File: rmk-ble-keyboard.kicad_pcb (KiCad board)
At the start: 2 copper layers, 57.8 x 48.1 mm, 1 part

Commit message: add matrix
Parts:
- added D1: 1N4148W, Diode_SMD:D_SOD-123, B.Cu at (41.2, 38.1)
- added D10: 1N4148W, Diode_SMD:D_SOD-123, B.Cu at (212.7, 38.1)
- added D11: 1N4148W, Diode_SMD:D_SOD-123, B.Cu at (231.7, 38.1)
- added D12: 1N4148W, Diode_SMD:D_SOD-123, B.Cu at (250.8, 38.1)
- added D13: 1N4148W, Diode_SMD:D_SOD-123, B.Cu at (269.8, 38.1)
- added D14: 1N4148W, Diode_SMD:D_SOD-123, B.Cu at (298.4, 38.1)
- added D15: 1N4148W, Diode_SMD:D_SOD-123, B.Cu at (46.0, 57.1)
- added D16: 1N4148W, Diode_SMD:D_SOD-123, B.Cu at (69.8, 57.1)
- added D17: 1N4148W, Diode_SMD:D_SOD-123, B.Cu at (88.8, 57.1)
- added D18: 1N4148W, Diode_SMD:D_SOD-123, B.Cu at (107.9, 57.1)
- added D19: 1N4148W, Diode_SMD:D_SOD-123, B.Cu at (126.9, 57.1)
- added D2: 1N4148W, Diode_SMD:D_SOD-123, B.Cu at (60.2, 38.1)
- added D20: 1N4148W, Diode_SMD:D_SOD-123, B.Cu at (146.0, 57.1)
- added D21: 1N4148W, Diode_SMD:D_SOD-123, B.Cu at (165.0, 57.1)
- added D22: 1N4148W, Diode_SMD:D_SOD-123, B.Cu at (184.1, 57.1)
- added D23: 1N4148W, Diode_SMD:D_SOD-123, B.Cu at (203.1, 57.1)
- added D24: 1N4148W, Diode_SMD:D_SOD-123, B.Cu at (222.2, 57.1)
- added D25: 1N4148W, Diode_SMD:D_SOD-123, B.Cu at (241.2, 57.1)
- added D26: 1N4148W, Diode_SMD:D_SOD-123, B.Cu at (260.3, 57.1)
- added D27: 1N4148W, Diode_SMD:D_SOD-123, B.Cu at (279.3, 57.1)
- added D28: 1N4148W, Diode_SMD:D_SOD-123, B.Cu at (303.1, 57.1)
- added D29: 1N4148W, Diode_SMD:D_SOD-123, B.Cu at (48.3, 76.2)
- added D3: 1N4148W, Diode_SMD:D_SOD-123, B.Cu at (79.3, 38.1)
- added D30: 1N4148W, Diode_SMD:D_SOD-123, B.Cu at (74.5, 76.2)
- added D31: 1N4148W, Diode_SMD:D_SOD-123, B.Cu at (93.6, 76.2)
- added D32: 1N4148W, Diode_SMD:D_SOD-123, B.Cu at (112.6, 76.2)
- added D33: 1N4148W, Diode_SMD:D_SOD-123, B.Cu at (131.7, 76.2)
- added D34: 1N4148W, Diode_SMD:D_SOD-123, B.Cu at (150.7, 76.2)
- added D35: 1N4148W, Diode_SMD:D_SOD-123, B.Cu at (169.8, 76.2)
- added D36: 1N4148W, Diode_SMD:D_SOD-123, B.Cu at (188.8, 76.2)
- added D37: 1N4148W, Diode_SMD:D_SOD-123, B.Cu at (207.9, 76.2)
- added D38: 1N4148W, Diode_SMD:D_SOD-123, B.Cu at (226.9, 76.2)
- added D39: 1N4148W, Diode_SMD:D_SOD-123, B.Cu at (246.0, 76.2)
- added D4: 1N4148W, Diode_SMD:D_SOD-123, B.Cu at (98.3, 38.1)
- added D40: 1N4148W, Diode_SMD:D_SOD-123, B.Cu at (265.0, 76.2)
- added D41: 1N4148W, Diode_SMD:D_SOD-123, B.Cu at (53.1, 95.2)
- added D42: 1N4148W, Diode_SMD:D_SOD-123, B.Cu at (296.0, 76.2)
- added D43: 1N4148W, Diode_SMD:D_SOD-123, B.Cu at (84.1, 95.2)
- added D44: 1N4148W, Diode_SMD:D_SOD-123, B.Cu at (103.1, 95.2)
- added D45: 1N4148W, Diode_SMD:D_SOD-123, B.Cu at (122.2, 95.2)
- added D46: 1N4148W, Diode_SMD:D_SOD-123, B.Cu at (141.2, 95.2)
- added D47: 1N4148W, Diode_SMD:D_SOD-123, B.Cu at (160.3, 95.2)
- added D48: 1N4148W, Diode_SMD:D_SOD-123, B.Cu at (179.3, 95.2)
- added D49: 1N4148W, Diode_SMD:D_SOD-123, B.Cu at (198.4, 95.2)
- added D5: 1N4148W, Diode_SMD:D_SOD-123, B.Cu at (117.4, 38.1)
- added D50: 1N4148W, Diode_SMD:D_SOD-123, B.Cu at (217.4, 95.2)
- added D51: 1N4148W, Diode_SMD:D_SOD-123, B.Cu at (236.5, 95.2)
- added D52: 1N4148W, Diode_SMD:D_SOD-123, B.Cu at (255.5, 95.2)
- added D53: 1N4148W, Diode_SMD:D_SOD-123, B.Cu at (291.2, 95.2)
- added D54: 1N4148W, Diode_SMD:D_SOD-123, B.Cu at (43.6, 114.3)
- added D55: 1N4148W, Diode_SMD:D_SOD-123, B.Cu at (67.4, 114.3)
- added D56: 1N4148W, Diode_SMD:D_SOD-123, B.Cu at (91.2, 114.3)
- added D57: 1N4148W, Diode_SMD:D_SOD-123, B.Cu at (162.6, 114.3)
- added D58: 1N4148W, Diode_SMD:D_SOD-123, B.Cu at (234.1, 114.3)
- added D59: 1N4148W, Diode_SMD:D_SOD-123, B.Cu at (257.9, 114.3)
- added D6: 1N4148W, Diode_SMD:D_SOD-123, B.Cu at (136.4, 38.1)
- added D60: 1N4148W, Diode_SMD:D_SOD-123, B.Cu at (281.7, 114.3)
- added D61: 1N4148W, Diode_SMD:D_SOD-123, B.Cu at (305.5, 114.3)
- added D7: 1N4148W, Diode_SMD:D_SOD-123, B.Cu at (155.5, 38.1)
- added D8: 1N4148W, Diode_SMD:D_SOD-123, B.Cu at (174.6, 38.1)
- added D9: 1N4148W, Diode_SMD:D_SOD-123, B.Cu at (193.6, 38.1)
- added SW1: esc, PCM_Switch_Keyboard_Hotswap_Kailh:SW_Hotswap_Kailh_MX_Plated_1.00u, F.Cu at (38.1, 38.1)
- added SW10: 9, PCM_Switch_Keyboard_Hotswap_Kailh:SW_Hotswap_Kailh_MX_Plated_1.00u, F.Cu at (209.6, 38.1)
- added SW11: 0, PCM_Switch_Keyboard_Hotswap_Kailh:SW_Hotswap_Kailh_MX_Plated_1.00u, F.Cu at (228.6, 38.1)
- added SW12: -, PCM_Switch_Keyboard_Hotswap_Kailh:SW_Hotswap_Kailh_MX_Plated_1.00u, F.Cu at (247.7, 38.1)
- added SW13: =, PCM_Switch_Keyboard_Hotswap_Kailh:SW_Hotswap_Kailh_MX_Plated_1.00u, F.Cu at (266.7, 38.1)
- added SW14: backspace, PCM_Switch_Keyboard_Hotswap_Kailh:SW_Hotswap_Kailh_MX_Plated_2.00u, F.Cu at (295.3, 38.1)
- added SW15: tab, PCM_Switch_Keyboard_Hotswap_Kailh:SW_Hotswap_Kailh_MX_Plated_1.50u, F.Cu at (42.9, 57.1)
- added SW16: q, PCM_Switch_Keyboard_Hotswap_Kailh:SW_Hotswap_Kailh_MX_Plated_1.00u, F.Cu at (66.7, 57.1)
- added SW17: w, PCM_Switch_Keyboard_Hotswap_Kailh:SW_Hotswap_Kailh_MX_Plated_1.00u, F.Cu at (85.7, 57.1)
- added SW18: e, PCM_Switch_Keyboard_Hotswap_Kailh:SW_Hotswap_Kailh_MX_Plated_1.00u, F.Cu at (104.8, 57.1)
- added SW19: r, PCM_Switch_Keyboard_Hotswap_Kailh:SW_Hotswap_Kailh_MX_Plated_1.00u, F.Cu at (123.8, 57.1)
- added SW2: 1, PCM_Switch_Keyboard_Hotswap_Kailh:SW_Hotswap_Kailh_MX_Plated_1.00u, F.Cu at (57.1, 38.1)
- added SW20: t, PCM_Switch_Keyboard_Hotswap_Kailh:SW_Hotswap_Kailh_MX_Plated_1.00u, F.Cu at (142.9, 57.1)
- added SW21: y, PCM_Switch_Keyboard_Hotswap_Kailh:SW_Hotswap_Kailh_MX_Plated_1.00u, F.Cu at (161.9, 57.1)
- added SW22: u, PCM_Switch_Keyboard_Hotswap_Kailh:SW_Hotswap_Kailh_MX_Plated_1.00u, F.Cu at (181.0, 57.1)
- added SW23: i, PCM_Switch_Keyboard_Hotswap_Kailh:SW_Hotswap_Kailh_MX_Plated_1.00u, F.Cu at (200.0, 57.1)
- added SW24: o, PCM_Switch_Keyboard_Hotswap_Kailh:SW_Hotswap_Kailh_MX_Plated_1.00u, F.Cu at (219.1, 57.1)
- added SW25: p, PCM_Switch_Keyboard_Hotswap_Kailh:SW_Hotswap_Kailh_MX_Plated_1.00u, F.Cu at (238.1, 57.1)
- added SW26: [, PCM_Switch_Keyboard_Hotswap_Kailh:SW_Hotswap_Kailh_MX_Plated_1.00u, F.Cu at (257.2, 57.1)
- added SW27: ], PCM_Switch_Keyboard_Hotswap_Kailh:SW_Hotswap_Kailh_MX_Plated_1.00u, F.Cu at (276.2, 57.1)
- added SW28: \, PCM_Switch_Keyboard_Hotswap_Kailh:SW_Hotswap_Kailh_MX_Plated_1.50u, F.Cu at (300.0, 57.1)
- added SW29: capslock, PCM_Switch_Keyboard_Hotswap_Kailh:SW_Hotswap_Kailh_MX_Plated_1.75u, F.Cu at (45.2, 76.2)
- added SW3: 2, PCM_Switch_Keyboard_Hotswap_Kailh:SW_Hotswap_Kailh_MX_Plated_1.00u, F.Cu at (76.2, 38.1)
- added SW30: a, PCM_Switch_Keyboard_Hotswap_Kailh:SW_Hotswap_Kailh_MX_Plated_1.00u, F.Cu at (71.4, 76.2)
- added SW31: s, PCM_Switch_Keyboard_Hotswap_Kailh:SW_Hotswap_Kailh_MX_Plated_1.00u, F.Cu at (90.5, 76.2)
- added SW32: d, PCM_Switch_Keyboard_Hotswap_Kailh:SW_Hotswap_Kailh_MX_Plated_1.00u, F.Cu at (109.5, 76.2)
- added SW33: f, PCM_Switch_Keyboard_Hotswap_Kailh:SW_Hotswap_Kailh_MX_Plated_1.00u, F.Cu at (128.6, 76.2)
- added SW34: g, PCM_Switch_Keyboard_Hotswap_Kailh:SW_Hotswap_Kailh_MX_Plated_1.00u, F.Cu at (147.6, 76.2)
- added SW35: h, PCM_Switch_Keyboard_Hotswap_Kailh:SW_Hotswap_Kailh_MX_Plated_1.00u, F.Cu at (166.7, 76.2)
- added SW36: j, PCM_Switch_Keyboard_Hotswap_Kailh:SW_Hotswap_Kailh_MX_Plated_1.00u, F.Cu at (185.7, 76.2)
- added SW37: k, PCM_Switch_Keyboard_Hotswap_Kailh:SW_Hotswap_Kailh_MX_Plated_1.00u, F.Cu at (204.8, 76.2)
- added SW38: l, PCM_Switch_Keyboard_Hotswap_Kailh:SW_Hotswap_Kailh_MX_Plated_1.00u, F.Cu at (223.8, 76.2)
- added SW39: ;, PCM_Switch_Keyboard_Hotswap_Kailh:SW_Hotswap_Kailh_MX_Plated_1.00u, F.Cu at (242.9, 76.2)
- added SW4: 3, PCM_Switch_Keyboard_Hotswap_Kailh:SW_Hotswap_Kailh_MX_Plated_1.00u, F.Cu at (95.2, 38.1)
- added SW40: ', PCM_Switch_Keyboard_Hotswap_Kailh:SW_Hotswap_Kailh_MX_Plated_1.00u, F.Cu at (261.9, 76.2)
- added SW41: enter, PCM_Switch_Keyboard_Hotswap_Kailh:SW_Hotswap_Kailh_MX_Plated_2.25u, F.Cu at (292.9, 76.2)
- added SW42: lshift, PCM_Switch_Keyboard_Hotswap_Kailh:SW_Hotswap_Kailh_MX_Plated_2.25u, F.Cu at (50.0, 95.2)
- added SW43: z, PCM_Switch_Keyboard_Hotswap_Kailh:SW_Hotswap_Kailh_MX_Plated_1.00u, F.Cu at (81.0, 95.2)
- added SW44: x, PCM_Switch_Keyboard_Hotswap_Kailh:SW_Hotswap_Kailh_MX_Plated_1.00u, F.Cu at (100.0, 95.2)
- added SW45: c, PCM_Switch_Keyboard_Hotswap_Kailh:SW_Hotswap_Kailh_MX_Plated_1.00u, F.Cu at (119.1, 95.2)
- added SW46: v, PCM_Switch_Keyboard_Hotswap_Kailh:SW_Hotswap_Kailh_MX_Plated_1.00u, F.Cu at (138.1, 95.2)
- added SW47: b, PCM_Switch_Keyboard_Hotswap_Kailh:SW_Hotswap_Kailh_MX_Plated_1.00u, F.Cu at (157.2, 95.2)
- added SW48: n, PCM_Switch_Keyboard_Hotswap_Kailh:SW_Hotswap_Kailh_MX_Plated_1.00u, F.Cu at (176.2, 95.2)
- added SW49: m, PCM_Switch_Keyboard_Hotswap_Kailh:SW_Hotswap_Kailh_MX_Plated_1.00u, F.Cu at (195.3, 95.2)
- added SW5: 4, PCM_Switch_Keyboard_Hotswap_Kailh:SW_Hotswap_Kailh_MX_Plated_1.00u, F.Cu at (114.3, 38.1)
- added SW50: ,, PCM_Switch_Keyboard_Hotswap_Kailh:SW_Hotswap_Kailh_MX_Plated_1.00u, F.Cu at (214.3, 95.2)
- added SW51: ., PCM_Switch_Keyboard_Hotswap_Kailh:SW_Hotswap_Kailh_MX_Plated_1.00u, F.Cu at (233.4, 95.2)
- added SW52: /, PCM_Switch_Keyboard_Hotswap_Kailh:SW_Hotswap_Kailh_MX_Plated_1.00u, F.Cu at (252.4, 95.2)
- added SW53: rshift, PCM_Switch_Keyboard_Hotswap_Kailh:SW_Hotswap_Kailh_MX_Plated_2.75u, F.Cu at (288.1, 95.2)
- added SW54: lctrl, PCM_Switch_Keyboard_Hotswap_Kailh:SW_Hotswap_Kailh_MX_Plated_1.25u, F.Cu at (40.5, 114.3)
- added SW55: lgui, PCM_Switch_Keyboard_Hotswap_Kailh:SW_Hotswap_Kailh_MX_Plated_1.25u, F.Cu at (64.3, 114.3)
- added SW56: lalt, PCM_Switch_Keyboard_Hotswap_Kailh:SW_Hotswap_Kailh_MX_Plated_1.25u, F.Cu at (88.1, 114.3)
- added SW57: space, PCM_Switch_Keyboard_Hotswap_Kailh:SW_Hotswap_Kailh_MX_Plated_6.25u, F.Cu at (159.5, 114.3)
- added SW58: ralt, PCM_Switch_Keyboard_Hotswap_Kailh:SW_Hotswap_Kailh_MX_Plated_1.25u, F.Cu at (231.0, 114.3)
- added SW59: rgui, PCM_Switch_Keyboard_Hotswap_Kailh:SW_Hotswap_Kailh_MX_Plated_1.25u, F.Cu at (254.8, 114.3)
- added SW6: 5, PCM_Switch_Keyboard_Hotswap_Kailh:SW_Hotswap_Kailh_MX_Plated_1.00u, F.Cu at (133.3, 38.1)
- added SW60: fn, PCM_Switch_Keyboard_Hotswap_Kailh:SW_Hotswap_Kailh_MX_Plated_1.25u, F.Cu at (278.6, 114.3)
- added SW61: rctrl, PCM_Switch_Keyboard_Hotswap_Kailh:SW_Hotswap_Kailh_MX_Plated_1.25u, F.Cu at (302.4, 114.3)
- added SW7: 6, PCM_Switch_Keyboard_Hotswap_Kailh:SW_Hotswap_Kailh_MX_Plated_1.00u, F.Cu at (152.4, 38.1)
- added SW8: 7, PCM_Switch_Keyboard_Hotswap_Kailh:SW_Hotswap_Kailh_MX_Plated_1.00u, F.Cu at (171.4, 38.1)
- added SW9: 8, PCM_Switch_Keyboard_Hotswap_Kailh:SW_Hotswap_Kailh_MX_Plated_1.00u, F.Cu at (190.5, 38.1)
- moved U1 92.4 mm to (153.1, 176.4)
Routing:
- net col2: track 0.00 -> 88.4 mm
- net col3: track 0.00 -> 86.4 mm
- net col10: track 0.00 -> 83.6 mm
- net col6: track 0.00 -> 83.6 mm
- net col11: track 0.00 -> 83.6 mm
- net col1: track 0.00 -> 81.6 mm
- net col13: track 0.00 -> 80.0 mm
- net col8: track 0.00 -> 63.6 mm
- net col5: track 0.00 -> 63.6 mm
- net col4: track 0.00 -> 63.6 mm
- net col9: track 0.00 -> 63.6 mm
- net col7: track 0.00 -> 63.6 mm
- net col14: track 0.00 -> 60.6 mm
- net col12: track 0.00 -> 41.7 mm
- net Net-(D61-A): track 0.00 -> 3.66 mm
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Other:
- board outline removed

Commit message: add usb & esd
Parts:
- added U2: USBLC6-2SC6, Package_TO_SOT_SMD:SOT-23-6, F.Cu at (203.6, 112.2)
- U1: moved to B.Cu
- moved U1 59.1 mm to (132.6, 120.9), turned to 180 degrees
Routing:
- net row4: track 0.00 -> 242.2 mm
- net row5: track 0.00 -> 48.4 mm
- net col14: track 60.6 -> 85.9 mm
- net col2: track 88.4 -> 89.9 mm
- net col3: track 86.4 -> 87.4 mm
- net col1: track 81.6 -> 82.4 mm
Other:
- board outline added: 285 x 94.5 mm

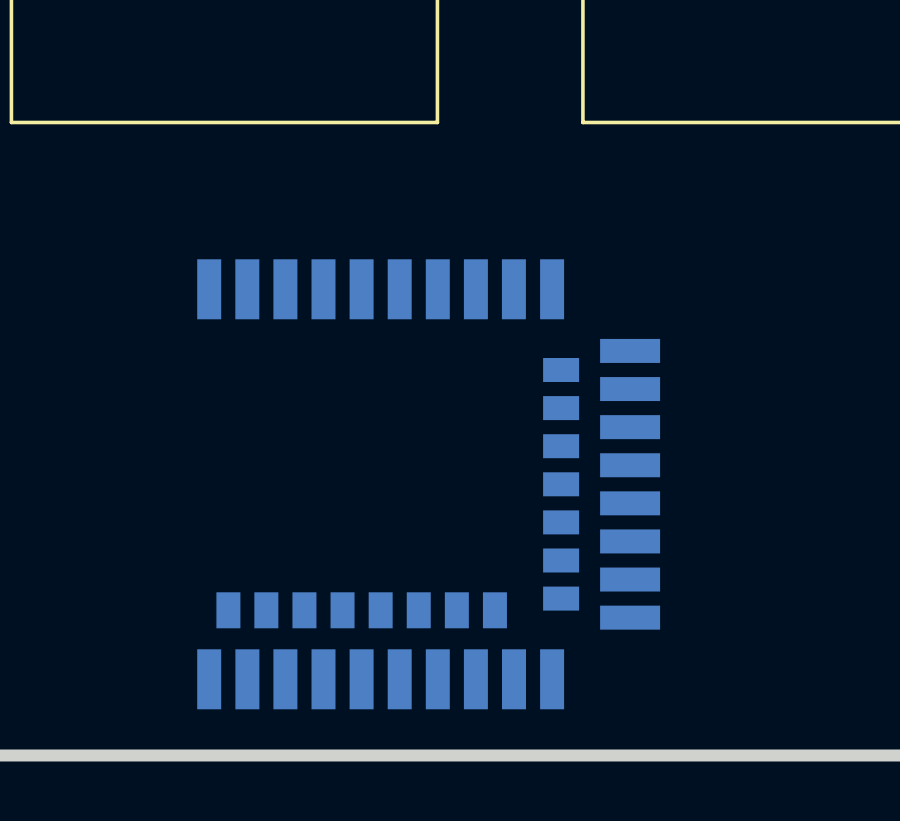
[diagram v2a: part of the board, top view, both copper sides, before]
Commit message: add e73 pin out in schema
Signed-off-by: HaoboGu <haobogu@outlook.com>
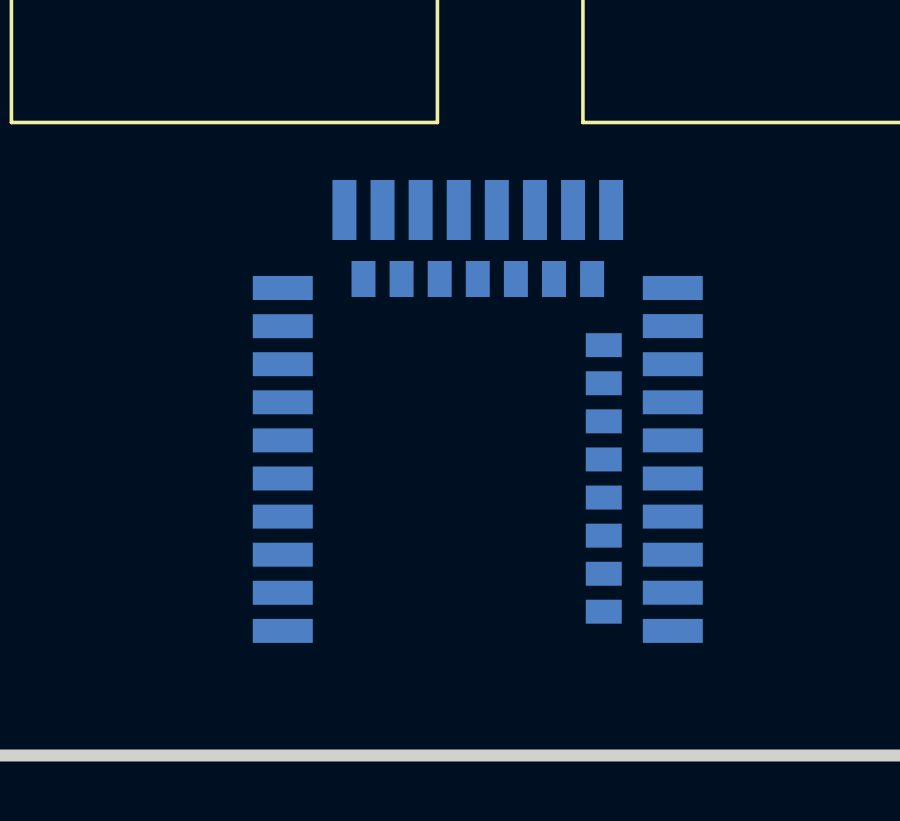
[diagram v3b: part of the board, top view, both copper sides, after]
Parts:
- moved U1 15.7 mm to (134.0, 105.3), turned to -90 degrees
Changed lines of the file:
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@@
 	(footprint "E73_2G4M08S1C:E73(2G4M08S1C)"
 		(layer "B.Cu")
-		(at 132.585 120.91 180)
+		(at 134.008 105.267 -90)
 		(property "Reference" "U1"
-			(at 8.525 14.7003 0)
+			(at 8.525 14.7003 90)
 			(unlocked yes)
 			(layer "B.SilkS")
@@
 		)
 		(property "Value" "~"
-			(at 8.525 -1.7003 0)
+			(at 8.525 -1.7003 90)
 			(unlocked yes)
 			(layer "B.Fab")
@@
 		)
 		(property "Footprint" "E73_2G4M08S1C:E73(2G4M08S1C)"
-			(at 0 0 0)
+			(at 0 0 90)
 			(unlocked yes)
 			(layer "B.Fab")
@@
 		)
 		(property "Datasheet" ""
-			(at 0 0 0)
+			(at 0 0 90)
 			(unlocked yes)
 			(layer "B.Fab")
@@
 		)
 		(property "Description" ""
-			(at 0 0 0)
+			(at 0 0 90)
 			(unlocked yes)
 			(layer "B.Fab")
@@
 		(sheetfile "rmk-ble-keyboard.kicad_sch")
 		(fp_line
-			(start 18 13)
-			(end 18 0)
+			(start 0 13)
+			(end 0 0)
 			(stroke
 				(width 0.1)
@@
 		)
 		(fp_line
+			(start 18 13)
+			(end 18 0)
+			(stroke
+				(width 0.1)
+				(type solid)
+			)
+			(layer "B.SilkS")
+		)
+		(fp_line
 			(start 18 0)
 			(end 0 0)
@@
 			(layer "B.SilkS")
 		)
-		(fp_line
-			(start 0 13)
-			(end 0 0)
-			(stroke
-				(width 0.1)
-				(type solid)
-			)
-			(layer "B.SilkS")
-		)
 		(pad "1" smd rect
-			(at 14.03 13 270)
+			(at 14.03 13)
 			(size 2 0.8)
 			(layers "B.Cu" "B.Paste" "B.Mask")
@@
 		)
 		(pad "2" smd rect
-			(at 12.76 13 270)
+			(at 12.76 13)
 			(size 2 0.8)
 			(layers "B.Cu" "B.Paste" "B.Mask")
@@
 		)
 		(pad "3" smd rect
-			(at 11.49 13 270)
+			(at 11.49 13)
 			(size 2 0.8)
 			(layers "B.Cu" "B.Paste" "B.Mask")
@@
 		)
 		(pad "4" smd rect
-			(at 10.22 13 270)
+			(at 10.22 13)
 			(size 2 0.8)
 			(layers "B.Cu" "B.Paste" "B.Mask")
@@
 		)
 		(pad "5" smd rect
-			(at 8.95 13 270)
+			(at 8.95 13)
 			(size 2 0.8)
 			(layers "B.Cu" "B.Paste" "B.Mask")
@@
 		)
 		(pad "6" smd rect
-			(at 7.68 13 270)
+			(at 7.68 13)
 			(size 2 0.8)
 			(layers "B.Cu" "B.Paste" "B.Mask")
@@
 		)
 		(pad "7" smd rect
-			(at 6.41 13 270)
+			(at 6.41 13)
 			(size 2 0.8)
 			(layers "B.Cu" "B.Paste" "B.Mask")
@@
 		)
 		(pad "8" smd rect
-			(at 5.14 13 270)
+			(at 5.14 13)
 			(size 2 0.8)
 			(layers "B.Cu" "B.Paste" "B.Mask")
@@
 		)
 		(pad "9" smd rect
-			(at 3.8728 13.0003 270)
+			(at 3.8728 13.0003)
 			(size 2 0.8)
 			(layers "B.Cu" "B.Paste" "B.Mask")
@@
 		)
 		(pad "10" smd rect
-			(at 2.6 13 270)
+			(at 2.6 13)
 			(size 2 0.8)
 			(layers "B.Cu" "B.Paste" "B.Mask")
@@
 		)
 		(pad "11" smd rect
-			(at 0 10.945 180)
+			(at 0 10.945 270)
 			(size 2 0.8)
 			(layers "B.Cu" "B.Paste" "B.Mask")
@@
 		)
 		(pad "12" smd rect
-			(at 2.3 10.30975 180)
+			(at 2.3 10.30975 270)
 			(size 1.2 0.8)
 			(layers "B.Cu" "B.Paste" "B.Mask")
@@
 		)
 		(pad "13" smd rect
-			(at 0 9.675 180)
+			(at 0 9.675 270)
 			(size 2 0.8)
 			(layers "B.Cu" "B.Paste" "B.Mask")
@@
 		)
 		(pad "14" smd rect
-			(at 2.3 9.03975 180)
+			(at 2.3 9.03975 270)
 			(size 1.2 0.8)
 			(layers "B.Cu" "B.Paste" "B.Mask")
@@
 		)
 		(pad "15" smd rect
-			(at 0 8.405 180)
+			(at 0 8.405 270)
 			(size 2 0.8)
 			(layers "B.Cu" "B.Paste" "B.Mask")
@@
 		)
 		(pad "16" smd rect
-			(at 2.3 7.76975 180)
+			(at 2.3 7.76975 270)
 			(size 1.2 0.8)
 			(layers "B.Cu" "B.Paste" "B.Mask")
@@
 		)
 		(pad "17" smd rect
-			(at 0 7.135 180)
+			(at 0 7.135 270)
 			(size 2 0.8)
 			(layers "B.Cu" "B.Paste" "B.Mask")
@@
 		)
 		(pad "18" smd rect
-			(at 2.3 6.49975 180)
+			(at 2.3 6.49975 270)
 			(size 1.2 0.8)
 			(layers "B.Cu" "B.Paste" "B.Mask")
@@
 		)
 		(pad "19" smd rect
-			(at 0 5.865 180)
+			(at 0 5.865 270)
 			(size 2 0.8)
 			(layers "B.Cu" "B.Paste" "B.Mask")
@@
 		)
 		(pad "20" smd rect
-			(at 2.3 5.22975 180)
+			(at 2.3 5.22975 270)
 			(size 1.2 0.8)
 			(layers "B.Cu" "B.Paste" "B.Mask")
@@
 		)
 		(pad "21" smd rect
-			(at 0 4.595 180)
+			(at 0 4.595 270)
 			(size 2 0.8)
 			(layers "B.Cu" "B.Paste" "B.Mask")
@@
 		)
 		(pad "22" smd rect
-			(at 2.3 3.95975 180)
+			(at 2.3 3.95975 270)
 			(size 1.2 0.8)
 			(layers "B.Cu" "B.Paste" "B.Mask")
@@
 		)
 		(pad "23" smd rect
-			(at 0 3.325 180)
+			(at 0 3.325 270)
 			(size 2 0.8)
 			(layers "B.Cu" "B.Paste" "B.Mask")
@@
 		)
 		(pad "24" smd rect
-			(at 2.3 2.69 180)
+			(at 2.3 2.69 270)
 			(size 1.2 0.8)
 			(layers "B.Cu" "B.Paste" "B.Mask")
@@
 		)
 		(pad "25" smd rect
-			(at 0 2.055 180)
+			(at 0 2.055 270)
 			(size 2 0.8)
 			(layers "B.Cu" "B.Paste" "B.Mask")
@@
 		)
 		(pad "26" smd rect
-			(at 2.6 0 90)
+			(at 2.6 0 180)
 			(size 2 0.8)
 			(layers "B.Cu" "B.Paste" "B.Mask")
@@
 		)
 		(pad "27" smd rect
-			(at 3.87 0 90)
+			(at 3.87 0 180)
 			(size 2 0.8)
 			(layers "B.Cu" "B.Paste" "B.Mask")
@@
 		)
 		(pad "28" smd rect
-			(at 4.505 2.3 270)
+			(at 4.505 2.3)
 			(size 1.2 0.8)
 			(layers "B.Cu" "B.Paste" "B.Mask")
@@
 		)
 		(pad "29" smd rect
-			(at 5.14 0 90)
+			(at 5.14 0 180)
 			(size 2 0.8)
 			(layers "B.Cu" "B.Paste" "B.Mask")
@@
 		)
 		(pad "30" smd rect
-			(at 5.775 2.3 270)
+			(at 5.775 2.3)
 			(size 1.2 0.8)
 			(layers "B.Cu" "B.Paste" "B.Mask")
@@
 		)
 		(pad "31" smd rect
-			(at 6.41 0 90)
+			(at 6.41 0 180)
 			(size 2 0.8)
 			(layers "B.Cu" "B.Paste" "B.Mask")
@@
 		)
 		(pad "32" smd rect
-			(at 7.045 2.3 270)
+			(at 7.045 2.3)
 			(size 1.2 0.8)
 			(layers "B.Cu" "B.Paste" "B.Mask")
@@
 		)
 		(pad "33" smd rect
-			(at 7.68 0 90)
+			(at 7.68 0 180)
 			(size 2 0.8)
 			(layers "B.Cu" "B.Paste" "B.Mask")
@@
 		)
 		(pad "34" smd rect
-			(at 8.315 2.3 270)
+			(at 8.315 2.3)
 			(size 1.2 0.8)
 			(layers "B.Cu" "B.Paste" "B.Mask")
@@
 		)
 		(pad "35" smd rect
-			(at 8.95 0 90)
+			(at 8.95 0 180)
 			(size 2 0.8)
 			(layers "B.Cu" "B.Paste" "B.Mask")
@@
 		)
 		(pad "36" smd rect
-			(at 9.585 2.3 270)
+			(at 9.585 2.3)
 			(size 1.2 0.8)
 			(layers "B.Cu" "B.Paste" "B.Mask")
@@
 		)
 		(pad "37" smd rect
-			(at 10.22 0 90)
+			(at 10.22 0 180)
 			(size 2 0.8)
 			(layers "B.Cu" "B.Paste" "B.Mask")
@@
 		)
 		(pad "38" smd rect
-			(at 10.855 2.3 270)
+			(at 10.855 2.3)
 			(size 1.2 0.8)
 			(layers "B.Cu" "B.Paste" "B.Mask")
@@
 		)
 		(pad "39" smd rect
-			(at 11.49 0 90)
+			(at 11.49 0 180)
 			(size 2 0.8)
 			(layers "B.Cu" "B.Paste" "B.Mask")
@@
 		)
 		(pad "40" smd rect
-			(at 12.125 2.3 270)
+			(at 12.125 2.3)
 			(size 1.2 0.8)
 			(layers "B.Cu" "B.Paste" "B.Mask")
@@
 		)
 		(pad "41" smd rect
-			(at 12.7572 -0.0003 90)
+			(at 12.7572 -0.0003 180)
 			(size 2 0.8)
 			(layers "B.Cu" "B.Paste" "B.Mask")
@@
 		)
 		(pad "42" smd rect
-			(at 13.39 2.3 270)
+			(at 13.39 2.3)
 			(size 1.2 0.8)
 			(layers "B.Cu" "B.Paste" "B.Mask")
@@
 		)
 		(pad "43" smd rect
-			(at 14.03 0 90)
-			(size 2 0.8)
-			(layers "B.Cu" "B.Paste" "B.Mask")
+			(at 14.03 0 180)
+			(size 2 0.8)
+			(layers "B.Cu" "B.Paste" "B.Mask")
